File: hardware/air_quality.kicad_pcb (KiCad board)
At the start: 2 copper layers, 20 x 25 mm, 26 parts, among them P101 CON-SENSOR2, P102 DEBUG, P103 BOOT, U1 BME680, U103 DRILL, U104 DRILL, U105 DRILL, U106 DRILL, U2 XMC1XXX48

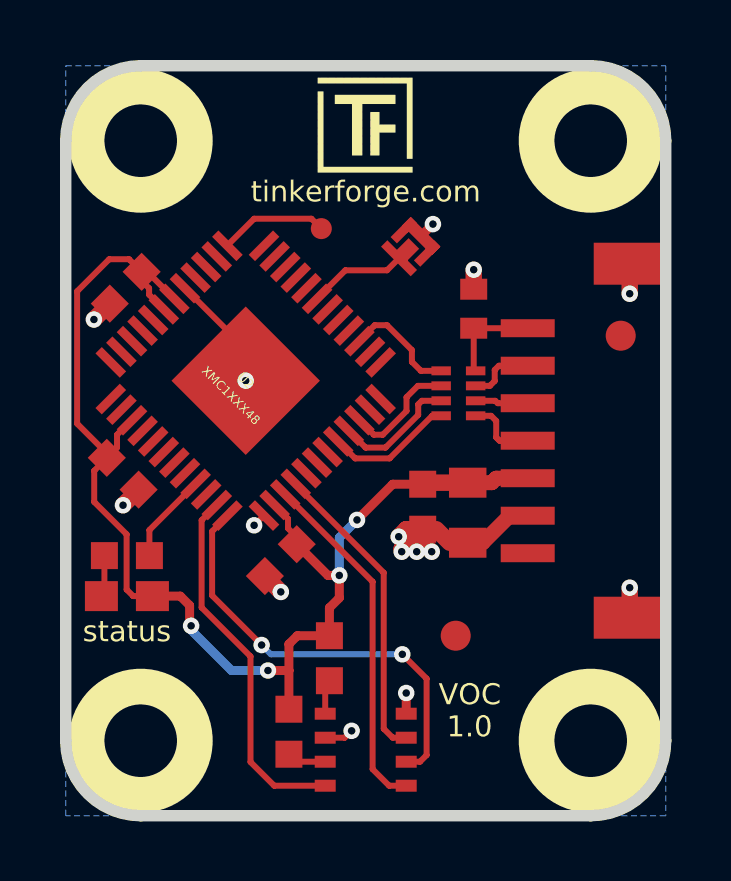
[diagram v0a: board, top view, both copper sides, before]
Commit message: rename voc bricklet to air quality bricklet
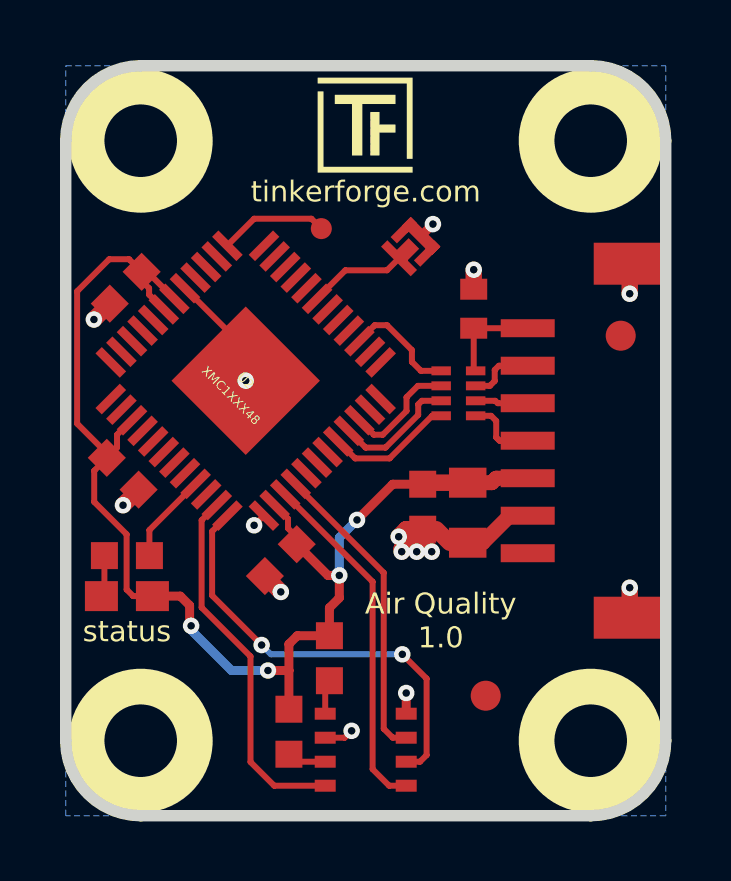
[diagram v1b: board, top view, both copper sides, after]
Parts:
- moved Fiducial_Mark 2.24 mm to (149.1, 149.5)
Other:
- board text added: "Air Quality 1.0"
- board text removed: "1.0"
- board text removed: "VOC"
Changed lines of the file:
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@@
-(kicad_pcb (version 4) (host pcbnew 4.0.2+dfsg1-stable)
+(kicad_pcb (version 4) (host pcbnew 4.0.7-e2-6376~58~ubuntu17.04.1)
   (general
     (links 48)
     (no_connects 0)
-    (area 134.244999 127.644999 275.56786 157.715)
+    (area 134.244999 127.644999 275.49286 158.115)
     (thickness 1.6)
-    (drawings 13)
+    (drawings 12)
     (tracks 209)
     (zones 0)
@@
   )
   (layers
-    (0 F.Cu signal)
-    (31 B.Cu signal)
+    (0 F.Cu signal hide)
+    (31 B.Cu signal hide)
     (32 B.Adhes user)
     (33 F.Adhes user)
@@
   )
   (module kicad-libraries:Fiducial_Mark (layer F.Cu)
-    (at 148.1 147.5)
+    (at 149.1 149.5)
     (attr smd)
     (fp_text reference Fiducial_Mark (at 0 0) (layer F.SilkS) hide
@@
     (effects (font (size 0.8 0.8) (thickness 0.15)))
   )
-  (gr_text 1.0 (at 148.56 150.53) (layer F.SilkS)
-    (effects (font (size 0.7 0.7) (thickness 0.15)))
-  )
   (gr_text status (at 137.14 147.36) (layer F.SilkS)
     (effects (font (size 0.7 0.7) (thickness 0.15)))
   )
-  (gr_text VOC (at 148.57 149.46) (layer F.SilkS)
+  (gr_text "Air Quality\n1.0" (at 147.6 147) (layer F.SilkS)
     (effects (font (size 0.7 0.7) (thickness 0.15)))
   )

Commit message: fix status text, set origin
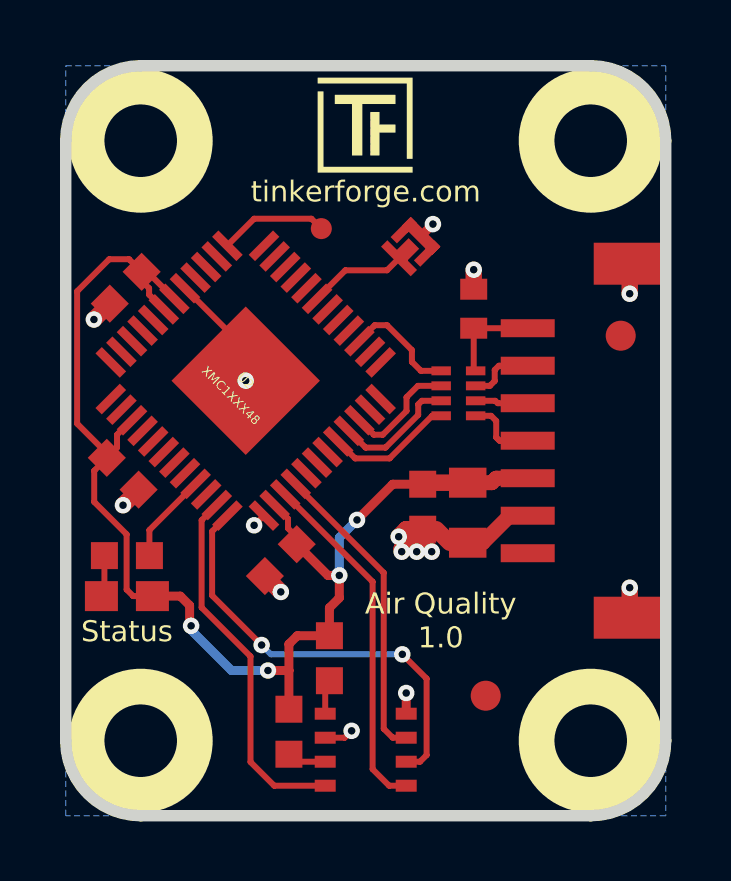
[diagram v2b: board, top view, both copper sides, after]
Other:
- board text added: "Status"
- board text removed: "status"
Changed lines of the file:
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@@
-(kicad_pcb (version 4) (host pcbnew 4.0.7-e2-6376~58~ubuntu17.04.1)
+(kicad_pcb (version 4) (host pcbnew 4.0.7-e2-6376~61~ubuntu18.04.1)
   (general
     (links 48)
@@
   )
   (layers
-    (0 F.Cu signal hide)
+    (0 F.Cu signal)
     (31 B.Cu signal hide)
     (32 B.Adhes user)
@@
     (pad_drill 0.6)
     (pad_to_mask_clearance 0)
-    (aux_axis_origin 0 0)
+    (aux_axis_origin 135.1 128.5)
+    (grid_origin 135.1 128.5)
     (visible_elements FFFFFF7F)
     (pcbplotparams
@@
     (effects (font (size 0.8 0.8) (thickness 0.15)))
   )
-  (gr_text status (at 137.14 147.36) (layer F.SilkS)
+  (gr_text Status (at 137.14 147.36) (layer F.SilkS)
     (effects (font (size 0.7 0.7) (thickness 0.15)))
   )

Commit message: fix wrong bypass capacitor connection, remove copper plane from sensor, increase sensor footprint pad size
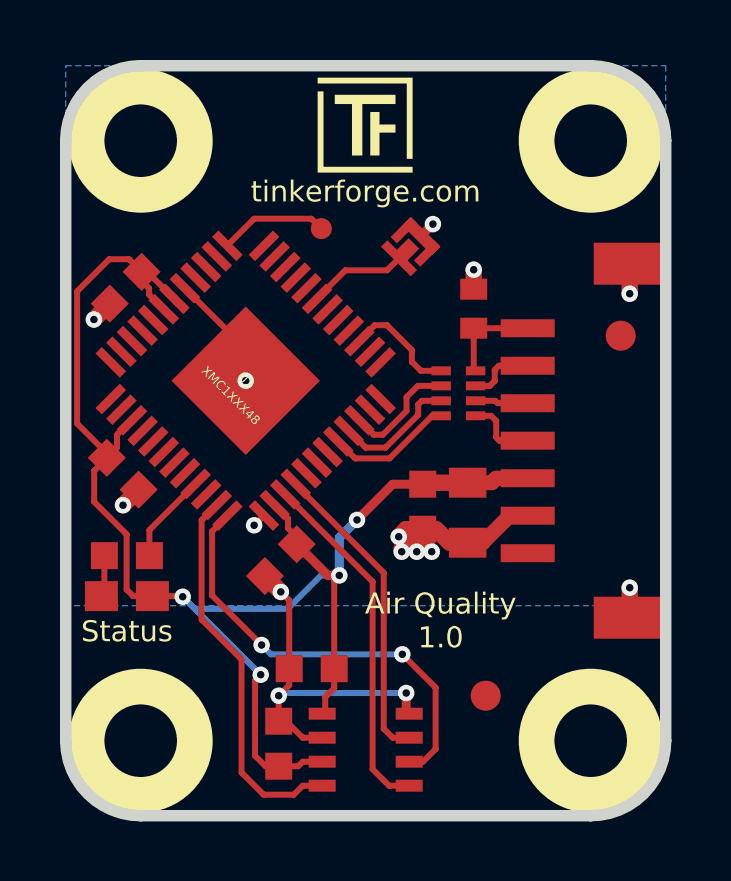
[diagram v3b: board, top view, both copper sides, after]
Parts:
- U1: footprint BME680 -> kicad-libraries:BME680
- moved C105 0.69 mm to (143.3, 148.6), turned to 180 degrees
- moved C1 0.52 mm to (142.2, 151.1), turned to 90 degrees
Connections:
- C1 pad 2: Net-(C1-Pad2) -> GND
- C105 pad 2: Net-(C105-Pad2) -> GND
- P101 pad 1: +5V -> (no net)
- U1 pad 6: Net-(C1-Pad2) -> VCC
- U1 pad 8: Net-(C105-Pad2) -> VCC
- U2 pad 1: Net-(U2-Pad1) -> (no net)
- U2 pad 10: Net-(U2-Pad10) -> (no net)
- U2 pad 11: Net-(U2-Pad11) -> (no net)
- U2 pad 12: Net-(U2-Pad12) -> (no net)
- U2 pad 14: Net-(U2-Pad14) -> (no net)
- U2 pad 15: Net-(U2-Pad15) -> (no net)
- U2 pad 16: Net-(U2-Pad16) -> (no net)
- U2 pad 2: Net-(U2-Pad2) -> (no net)
- U2 pad 20: Net-(U2-Pad20) -> (no net)
- U2 pad 21: Net-(U2-Pad21) -> (no net)
- U2 pad 22: Net-(U2-Pad22) -> (no net)
- U2 pad 23: Net-(U2-Pad23) -> (no net)
- U2 pad 24: Net-(U2-Pad24) -> (no net)
- U2 pad 25: Net-(U2-Pad25) -> (no net)
- U2 pad 26: Net-(U2-Pad26) -> (no net)
- U2 pad 28: Net-(U2-Pad28) -> (no net)
- U2 pad 29: Net-(U2-Pad29) -> (no net)
- U2 pad 30: Net-(U2-Pad30) -> (no net)
- U2 pad 31: Net-(U2-Pad31) -> (no net)
- U2 pad 32: Net-(U2-Pad32) -> (no net)
- U2 pad 34: Net-(U2-Pad34) -> (no net)
- U2 pad 4: Net-(U2-Pad4) -> (no net)
- U2 pad 41: Net-(U2-Pad41) -> (no net)
- U2 pad 42: Net-(U2-Pad42) -> (no net)
- U2 pad 43: Net-(U2-Pad43) -> (no net)
- U2 pad 47: Net-(U2-Pad47) -> (no net)
- U2 pad 48: Net-(U2-Pad48) -> (no net)
- U2 pad 5: Net-(U2-Pad5) -> (no net)
- U2 pad 6: Net-(U2-Pad6) -> (no net)
- U2 pad 8: Net-(U2-Pad8) -> (no net)
- U2 pad 9: Net-(U2-Pad9) -> (no net)
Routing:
- net GND: track 21.2 -> 31.0 mm
- net VCC: track 43.0 -> 51.3 mm
- net Net-(C1-Pad2): track 1.31 -> 0.00 mm
- net Net-(C105-Pad2): track 1.16 -> 0.00 mm
- net M-MISO: track 12.3 -> 12.9 mm
